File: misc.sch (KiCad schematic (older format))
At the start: 15 parts, among them U1 SAMA5D2x-SIP, Y1 NX2016SA_24MHz, Y2 NX2012SA_32-768KHz

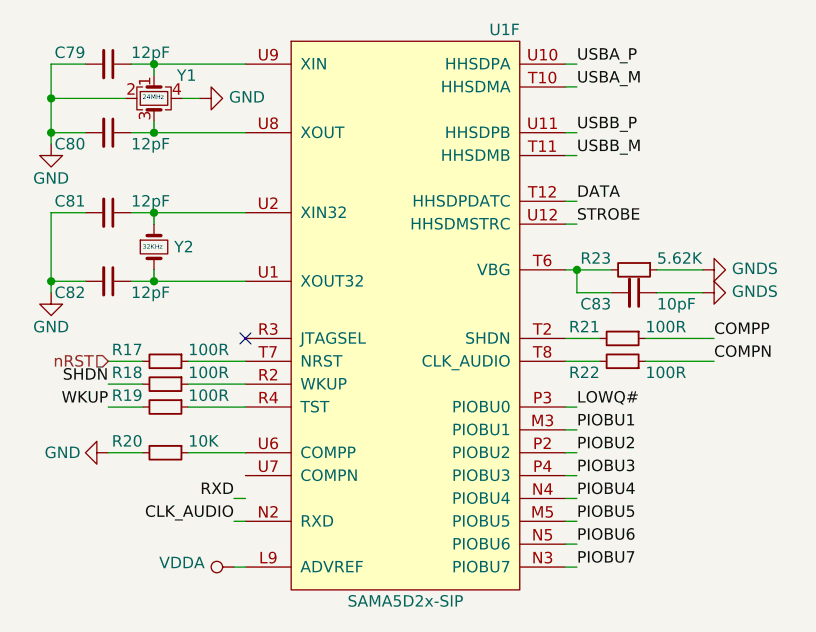
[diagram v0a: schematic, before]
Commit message: Finished power, added microSD, USB A, btn
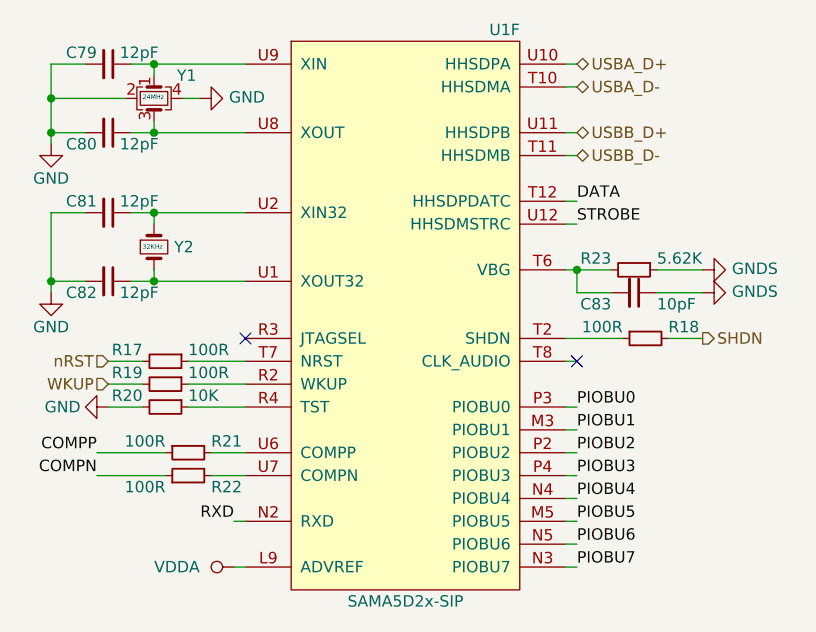
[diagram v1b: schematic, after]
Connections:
- net CLK_AUDIO is gone; now on net RXD: U1.N2 (RXD)
- net at U1.R2 (WKUP): now also R19.1; no longer R18.1
- net at U1.R4 (TST): now also R20.1; no longer R19.1
- net at U1.T2 (SHDN): now also R18.1; no longer R21.2
- net at U1.T8 (CLK_AUDIO): no longer R22.2
- net at U1.U6 (COMPP): now also R21.2; no longer R20.1
- net at U1.U7 (COMPN): now also R22.2
- net LOWQ# renamed PIOBU0
- net USBA_M renamed USBA_D-
- net USBA_P renamed USBA_D+
- net USBB_M renamed USBB_D-
- net USBB_P renamed USBB_D+
- no-connect marks 1 -> 2
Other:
- moved on the sheet: R18, R19, R20, R21, R22
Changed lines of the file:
@@
 	6500 3400 6550 3400
 Wire Wire Line
-	6500 3900 6650 3900
+	5100 4400 4950 4400
 Wire Wire Line
 	6500 4200 6550 4200
@@
 Wire Wire Line
 	6500 4900 6550 4900
-Text Label 6550 2700 0    50   ~ 0
-USBA_P
-Text Label 6550 2800 0    50   ~ 0
-USBA_M
-Text Label 6550 3000 0    50   ~ 0
-USBB_P
-Text Label 6550 3100 0    50   ~ 0
-USBB_M
 Text Label 6550 3300 0    50   ~ 0
 DATA
@@
 STROBE
 Text Label 6550 4200 0    50   ~ 0
-LOWQ#
+PIOBU0
 Text Label 6550 4300 0    50   ~ 0
 PIOBU1
@@
 L Device:R_Small R?
 U 1 1 5DABE39B
-P 6750 3900
+P 4850 4400
 AR Path="/5DABE39B" Ref="R?"  Part="1"
 AR Path="/5DAA7CAC/5DABE39B" Ref="R21"  Part="1"
-F 0 "R21" V 6700 3800 50  0000 R CNN
-F 1 "100R" V 6700 4000 50  0000 L CNN
-F 2 "" H 6750 3900 50  0001 C CNN
-F 3 "~" H 6750 3900 50  0001 C CNN
-	1    6750 3900
-	0    1    1    0
+F 0 "R21" V 4800 4300 50  0000 R CNN
+F 1 "100R" V 4800 4500 50  0000 L CNN
+F 2 "" H 4850 4400 50  0001 C CNN
+F 3 "~" H 4850 4400 50  0001 C CNN
+	1    4850 4400
+	0    -1   1    0
 $EndComp
 $Comp
 L Device:R_Small R?
 U 1 1 5DABE3A1
-P 6750 4000
+P 4850 4500
 AR Path="/5DABE3A1" Ref="R?"  Part="1"
 AR Path="/5DAA7CAC/5DABE3A1" Ref="R22"  Part="1"
-F 0 "R22" V 6700 3900 50  0000 R CNN
-F 1 "100R" V 6700 4100 50  0000 L CNN
-F 2 "" H 6750 4000 50  0001 C CNN
-F 3 "~" H 6750 4000 50  0001 C CNN
-	1    6750 4000
-	0    1    -1   0
-$EndComp
-Wire Wire Line
-	6500 4000 6650 4000
-Wire Wire Line
-	6850 3900 7150 3900
-Wire Wire Line
-	6850 4000 7150 4000
-Text Label 7150 3900 0    50   ~ 0
+F 0 "R22" V 4800 4400 50  0000 R CNN
+F 1 "100R" V 4800 4600 50  0000 L CNN
+F 2 "" H 4850 4500 50  0001 C CNN
+F 3 "~" H 4850 4500 50  0001 C CNN
+	1    4850 4500
+	0    -1   -1   0
+$EndComp
+Wire Wire Line
+	5100 4500 4950 4500
+Wire Wire Line
+	4750 4400 4450 4400
+Wire Wire Line
+	4750 4500 4450 4500
+Text Label 4450 4400 2    50   ~ 0
 COMPP
-Text Label 7150 4000 0    50   ~ 0
+Text Label 4450 4500 2    50   ~ 0
 COMPN
 Wire Wire Line
@@
 AR Path="/5DABE3DA" Ref="C?"  Part="1"
 AR Path="/5DAA7CAC/5DABE3DA" Ref="C79"  Part="1"
-F 0 "C79" V 4450 2600 50  0000 R CNN
-F 1 "12pF" V 4450 2800 50  0000 L CNN
+F 0 "C79" V 4450 2650 50  0000 R CNN
+F 1 "12pF" V 4450 2750 50  0000 L CNN
 F 2 "" H 4500 2700 50  0001 C CNN
 F 3 "~" H 4500 2700 50  0001 C CNN
@@
 AR Path="/5DABE3E1" Ref="C?"  Part="1"
 AR Path="/5DAA7CAC/5DABE3E1" Ref="C80"  Part="1"
-F 0 "C80" V 4450 2900 50  0000 R CNN
-F 1 "12pF" V 4450 3100 50  0000 L CNN
+F 0 "C80" V 4450 2950 50  0000 R CNN
+F 1 "12pF" V 4450 3050 50  0000 L CNN
 F 2 "" H 4500 3000 50  0001 C CNN
 F 3 "~" H 4500 3000 50  0001 C CNN
@@
 AR Path="/5DABE407" Ref="C?"  Part="1"
 AR Path="/5DAA7CAC/5DABE407" Ref="C82"  Part="1"
-F 0 "C82" V 4450 3550 50  0000 R CNN
-F 1 "12pF" V 4450 3750 50  0000 L CNN
+F 0 "C82" V 4450 3600 50  0000 R CNN
+F 1 "12pF" V 4450 3700 50  0000 L CNN
 F 2 "" H 4500 3650 50  0001 C CNN
 F 3 "~" H 4500 3650 50  0001 C CNN
@@
 AR Path="/5DABE40E" Ref="C?"  Part="1"
 AR Path="/5DAA7CAC/5DABE40E" Ref="C81"  Part="1"
-F 0 "C81" V 4450 3250 50  0000 R CNN
-F 1 "12pF" V 4450 3450 50  0000 L CNN
+F 0 "C81" V 4450 3300 50  0000 R CNN
+F 1 "12pF" V 4450 3400 50  0000 L CNN
 F 2 "" H 4500 3350 50  0001 C CNN
 F 3 "~" H 4500 3350 50  0001 C CNN
@@
 L Device:R_Small R?
 U 1 1 5DABE42F
-P 4750 4200
+P 4750 4100
 AR Path="/5DABE42F" Ref="R?"  Part="1"
 AR Path="/5DAA7CAC/5DABE42F" Ref="R19"  Part="1"
-F 0 "R19" V 4700 4100 50  0000 R CNN
-F 1 "100R" V 4700 4300 50  0000 L CNN
-F 2 "" H 4750 4200 50  0001 C CNN
-F 3 "~" H 4750 4200 50  0001 C CNN
-	1    4750 4200
-	0    1    1    0
-$EndComp
-Wire Wire Line
-	4850 4200 5100 4200
-Wire Wire Line
-	4650 4200 4500 4200
-Text Label 4500 4200 2    50   ~ 0
-WKUP
-$Comp
-L Device:R_Small R?
-U 1 1 5DABE438
-P 4750 4400
-AR Path="/5DABE438" Ref="R?"  Part="1"
-AR Path="/5DAA7CAC/5DABE438" Ref="R20"  Part="1"
-F 0 "R20" V 4700 4300 50  0000 R CNN
-F 1 "10K" V 4700 4500 50  0000 L CNN
-F 2 "" H 4750 4400 50  0001 C CNN
-F 3 "~" H 4750 4400 50  0001 C CNN
-	1    4750 4400
-	0    1    1    0
-$EndComp
-Wire Wire Line
-	4850 4400 5100 4400
-Wire Wire Line
-	4650 4400 4500 4400
-$Comp
-L power:GND #PWR?
-U 1 1 5DABE440
-P 4500 4400
-AR Path="/5DABE440" Ref="#PWR?"  Part="1"
-AR Path="/5DAA7CAC/5DABE440" Ref="#PWR0188"  Part="1"
-F 0 "#PWR0188" H 4500 4150 50  0001 C CNN
-F 1 "GND" V 4500 4200 50  0000 C CNN
-F 2 "" H 4500 4400 50  0001 C CNN
-F 3 "" H 4500 4400 50  0001 C CNN
-	1    4500 4400
-	0    1    1    0
-$EndComp
-Wire Wire Line
-	5100 4100 4850 4100
-$Comp
-L Device:R_Small R?
-U 1 1 5DABE447
-P 4750 4100
-AR Path="/5DABE447" Ref="R?"  Part="1"
-AR Path="/5DAA7CAC/5DABE447" Ref="R18"  Part="1"
-F 0 "R18" V 4700 4000 50  0000 R CNN
+F 0 "R19" V 4700 4000 50  0000 R CNN
 F 1 "100R" V 4700 4200 50  0000 L CNN
 F 2 "" H 4750 4100 50  0001 C CNN
@@
 $EndComp
 Wire Wire Line
+	4850 4100 5100 4100
+Wire Wire Line
 	4650 4100 4500 4100
-Text Label 4500 4100 2    50   ~ 0
-SHDN
-Wire Wire Line
-	5100 4600 5050 4600
+$Comp
+L Device:R_Small R?
+U 1 1 5DABE438
+P 4750 4200
+AR Path="/5DABE438" Ref="R?"  Part="1"
+AR Path="/5DAA7CAC/5DABE438" Ref="R20"  Part="1"
+F 0 "R20" V 4700 4100 50  0000 R CNN
+F 1 "10K" V 4700 4300 50  0000 L CNN
+F 2 "" H 4750 4200 50  0001 C CNN
+F 3 "~" H 4750 4200 50  0001 C CNN
+	1    4750 4200
+	0    1    1    0
+$EndComp
+Wire Wire Line
+	4850 4200 5100 4200
+Wire Wire Line
+	4650 4200 4500 4200
+$Comp
+L power:GND #PWR?
+U 1 1 5DABE440
+P 4500 4200
+AR Path="/5DABE440" Ref="#PWR?"  Part="1"
+AR Path="/5DAA7CAC/5DABE440" Ref="#PWR0188"  Part="1"
+F 0 "#PWR0188" H 4500 3950 50  0001 C CNN
+F 1 "GND" V 4500 4000 50  0000 C CNN
+F 2 "" H 4500 4200 50  0001 C CNN
+F 3 "" H 4500 4200 50  0001 C CNN
+	1    4500 4200
+	0    1    1    0
+$EndComp
+Wire Wire Line
+	6500 3900 6750 3900
+$Comp
+L Device:R_Small R?
+U 1 1 5DABE447
+P 6850 3900
+AR Path="/5DABE447" Ref="R?"  Part="1"
+AR Path="/5DAA7CAC/5DABE447" Ref="R18"  Part="1"
+F 0 "R18" V 6800 3800 50  0000 R CNN
+F 1 "100R" V 6800 4000 50  0000 L CNN
+F 2 "" H 6850 3900 50  0001 C CNN
+F 3 "~" H 6850 3900 50  0001 C CNN
+	1    6850 3900
+	0    -1   1    0
+$EndComp
+Wire Wire Line
+	6950 3900 7100 3900
 Wire Wire Line
 	5100 4700 5050 4700
 Wire Wire Line
+	6500 4000 6550 4000
+Wire Wire Line
 	5100 4900 5050 4900
-Text Label 5050 4600 2    50   ~ 0
-RXD
-Text Label 5050 4700 2    50   ~ 0
-CLK_AUDIO
 $Comp
 L power:VDDA #PWR?
@@
 AR Path="/5DAA7CAC/5DABE454" Ref="#PWR0189"  Part="1"
 F 0 "#PWR0189" H 5050 4750 50  0001 C CNN
-F 1 "VDDA" V 5068 5028 50  0000 L CNN
+F 1 "VDDA" V 5050 5050 50  0000 L CNN
 F 2 "" H 5050 4900 50  0001 C CNN
 F 3 "" H 5050 4900 50  0001 C CNN
@@
 Text HLabel 4500 4000 0    50   Input ~ 0
 nRST
+Text HLabel 7100 3900 2    50   Output ~ 0
+SHDN
+Text HLabel 4500 4100 0    50   Input ~ 0
+WKUP
+Text Label 5050 4700 2    50   ~ 0
+RXD
+NoConn ~ 6550 4000
+Text HLabel 6550 2700 2    50   BiDi ~ 0
+USBA_D+
+Text HLabel 6550 2800 2    50   BiDi ~ 0
+USBA_D-
+Text HLabel 6550 3000 2    50   BiDi ~ 0
+USBB_D+
+Text HLabel 6550 3100 2    50   BiDi ~ 0
+USBB_D-
 $EndSCHEMATC

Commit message: Finish schematic (?), set footprints and start placement
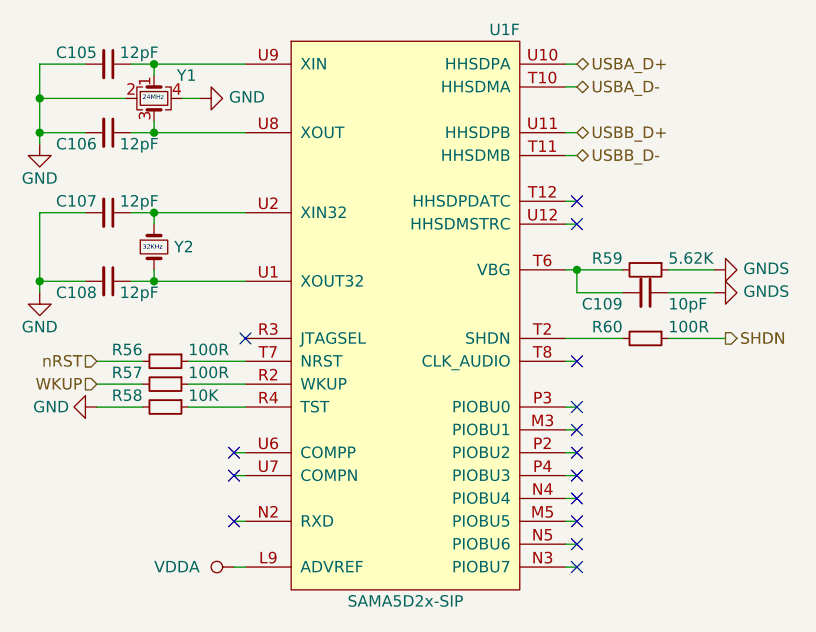
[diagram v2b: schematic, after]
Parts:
- removed R21, R22: 100R, symbol Device:R_Small
- C105: renamed from C79; footprint (none) -> Capacitor_SMD:C_0402_1005Metric
- C106: renamed from C80; footprint (none) -> Capacitor_SMD:C_0402_1005Metric
- C107: renamed from C81; footprint (none) -> Capacitor_SMD:C_0402_1005Metric
- C108: renamed from C82; footprint (none) -> Capacitor_SMD:C_0402_1005Metric
- C109: renamed from C83; footprint (none) -> Capacitor_SMD:C_0402_1005Metric
- R56: renamed from R17; footprint (none) -> Resistor_SMD:R_0603_1608Metric
- R57: renamed from R19; footprint (none) -> Resistor_SMD:R_0603_1608Metric
- R58: renamed from R20; footprint (none) -> Resistor_SMD:R_0603_1608Metric
- R59: renamed from R23; footprint (none) -> Resistor_SMD:R_0603_1608Metric
- R60: renamed from R18; footprint (none) -> Resistor_SMD:R_0603_1608Metric
- Y1: footprint (none) -> Crystal:Crystal_SMD_2016-4Pin_2.0x1.6mm
- Y2: footprint (none) -> Crystal:Crystal_SMD_2012-2Pin_2.0x1.2mm
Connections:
- net SHDN: now also R60.1; no longer R60.2
- net at U1.T2 (SHDN): now also R60.2; no longer R60.1
- net DATA: no longer names the net of U1.T12 (HHSDPDATC)
- net PIOBU0: no longer names the net of U1.P3 (PIOBU0)
- net PIOBU1: no longer names the net of U1.M3 (PIOBU1)
- net PIOBU2: no longer names the net of U1.P2 (PIOBU2)
- net PIOBU3: no longer names the net of U1.P4 (PIOBU3)
- net PIOBU4: no longer names the net of U1.N4 (PIOBU4)
- net PIOBU5: no longer names the net of U1.M5 (PIOBU5)
- net PIOBU6: no longer names the net of U1.N5 (PIOBU6)
- net PIOBU7: no longer names the net of U1.N3 (PIOBU7)
- net RXD: no longer names the net of U1.N2 (RXD)
- net STROBE: no longer names the net of U1.U12 (HHSDMSTRC)
- no-connect marks 2 -> 15
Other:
- moved on the sheet: C109, R59

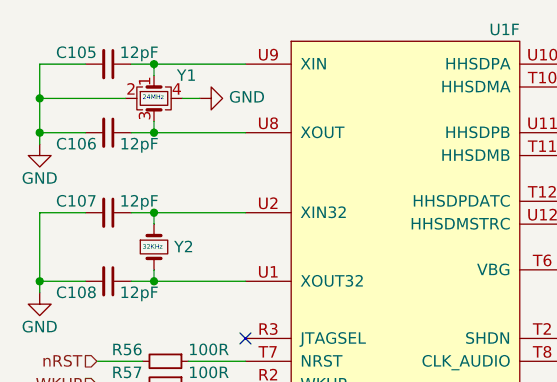
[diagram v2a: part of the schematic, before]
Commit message: More routing, 165 unconnected left
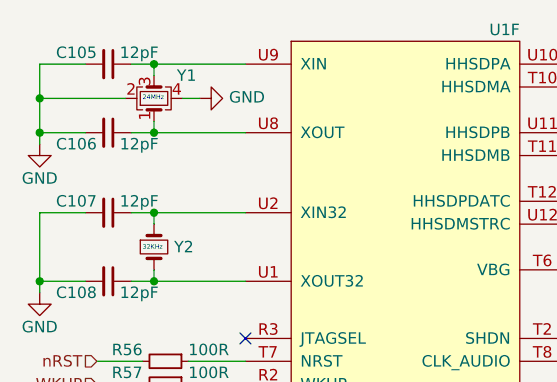
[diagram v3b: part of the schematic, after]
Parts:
- Y1: value NX2016SA_24MHz -> TSX-3225 24MHz; footprint Crystal:Crystal_SMD_2016-4Pin_2.0x1.6mm -> Crystal:Crystal_SMD_3225-4Pin_3.2x2.5mm
- Y2: value NX2012SA_32-768KHz -> 32kHz; footprint Crystal:Crystal_SMD_2012-2Pin_2.0x1.2mm -> Crystal:Crystal_SMD_3215-2Pin_3.2x1.5mm
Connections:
- net at C106.1, U1.U8 (XOUT): now also Y1.1; no longer Y1.3
- net at C105.1, U1.U9 (XIN): now also Y1.3; no longer Y1.1
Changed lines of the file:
@@
 AR Path="/5DABE3CB" Ref="Y?"  Part="1"
 AR Path="/5DAA7CAC/5DABE3CB" Ref="Y1"  Part="1"
-F 0 "Y1" V 4600 2950 50  0000 L CNN
-F 1 "NX2016SA_24MHz" H 4844 2805 50  0001 L CNN
-F 2 "Crystal:Crystal_SMD_2016-4Pin_2.0x1.6mm" H 4700 2850 50  0001 C CNN
+F 0 "Y1" V 4800 2950 50  0000 L CNN
+F 1 "TSX-3225 24MHz" H 4844 2805 50  0001 L CNN
+F 2 "Crystal:Crystal_SMD_3225-4Pin_3.2x2.5mm" H 4700 2850 50  0001 C CNN
 F 3 "~" H 4700 2850 50  0001 C CNN
 	1    4700 2850
-	0    1    1    0
+	0    1    -1   0
 $EndComp
 Wire Wire Line
@@
 AR Path="/5DAA7CAC/5DABE3FD" Ref="Y2"  Part="1"
 F 0 "Y2" V 4700 3588 50  0000 L CNN
-F 1 "NX2012SA_32-768KHz" V 4745 3588 50  0001 L CNN
-F 2 "Crystal:Crystal_SMD_2012-2Pin_2.0x1.2mm" H 4700 3500 50  0001 C CNN
+F 1 "32kHz" V 4745 3588 50  0001 L CNN
+F 2 "Crystal:Crystal_SMD_3215-2Pin_3.2x1.5mm" H 4700 3500 50  0001 C CNN
 F 3 "~" H 4700 3500 50  0001 C CNN
 	1    4700 3500
